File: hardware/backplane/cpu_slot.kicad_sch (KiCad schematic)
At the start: 1 part

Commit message: feat: Re-add peripheral MCLK, add to memory lines (#3)
Need MCLK to maintain peripheral synchronization.  Add missing memory
access size and latch lines.
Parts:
- renumbered J9 to J8
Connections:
- net UART.RX is gone; now on an unnamed net: J8.B13
- net UART.TX is gone; now on net MCLK: J8.B12
- net GND: no longer J8.A16
- net MCLK: no longer J8.B18
- net ~{MRST}: now also J8.A16; no longer J8.B17
- net at J8.B1, J8.B49, J8.B82: no longer J8.B16
- net I2C.SCL: no longer names the net of J8.B14
- net I2C.SDA: no longer names the net of J8.B15
- new net MEM.BYTE: J8.B18
- new net MEM.HALFWORD: J8.B17
- new net MEM.LATCH: J8.B16
- no-connect marks 17 -> 19

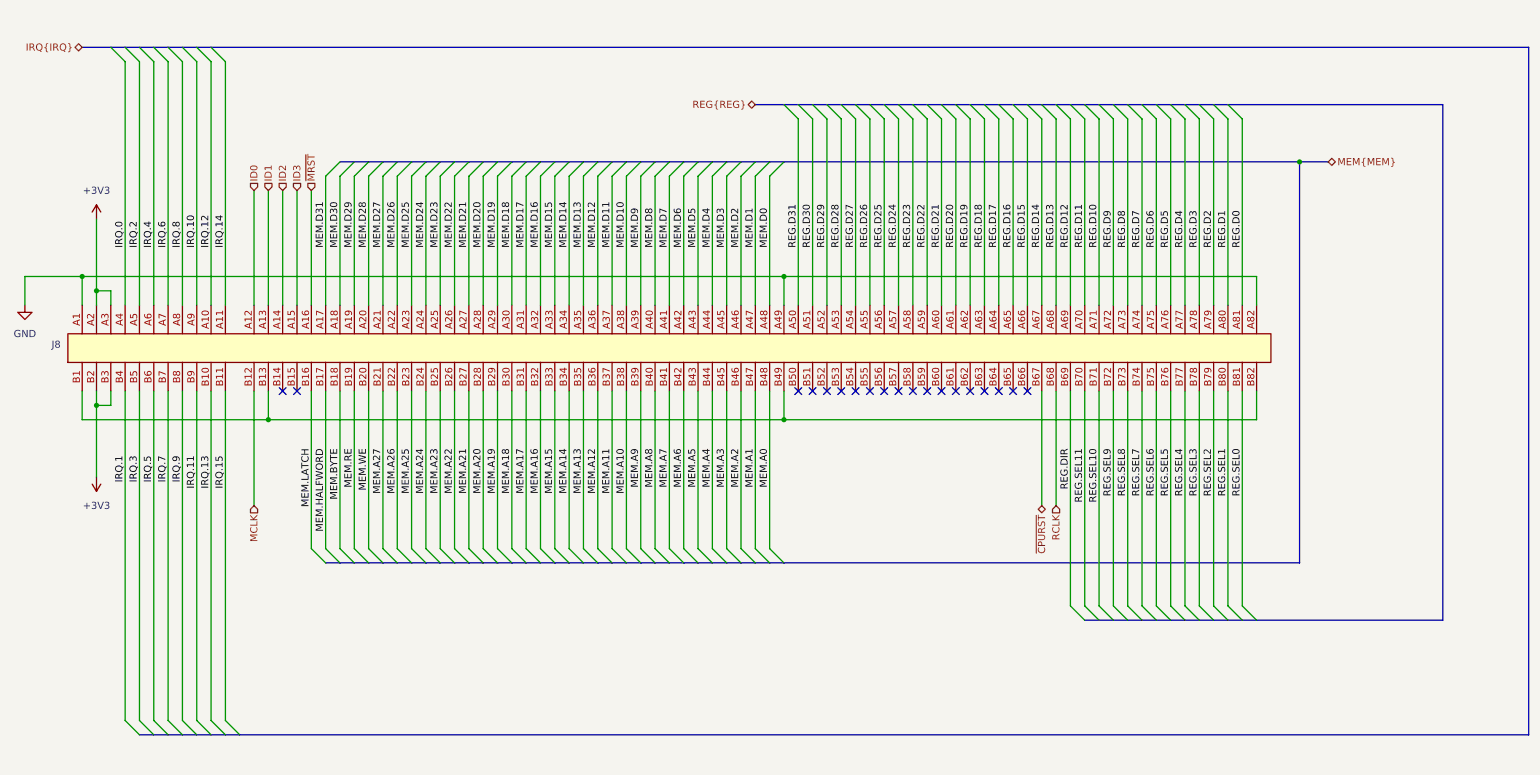
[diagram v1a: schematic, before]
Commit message: feat: Assign footprints, add testpoints
 * Verify all footprints are assigned.
 * Create testpoints for key signals.
 * Reorganize component libraries.
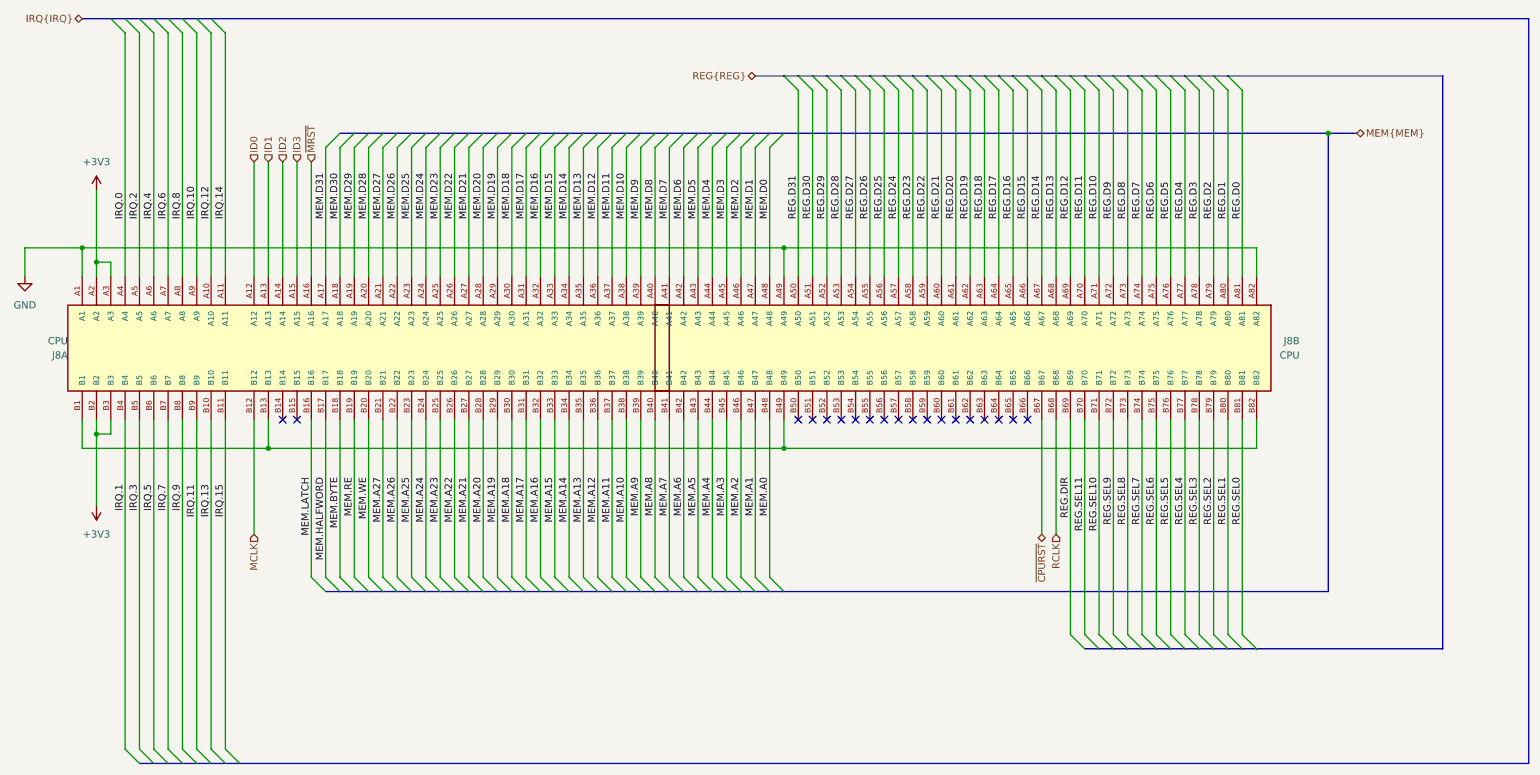
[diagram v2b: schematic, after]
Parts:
- removed J8: ~, symbol Connector_PCIe:PCIe_x16
- added J8: CPU, 10018783_10113TLF:AMPHENOL_10018783-10113TLF, symbol 10018783-10113TLF:10018783-10113TLF
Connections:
- net +3V3: now also J8.A2, J8.A3, J8.B2, J8.B3
- net GND: now also J8.A1, J8.A49, J8.A82
- net ID0: now also J8.A12
- net ID1: now also J8.A13
- net ID2: now also J8.A14
- net ID3: now also J8.A15
- net IRQ.0: now also J8.A4
- net IRQ.1: now also J8.B4
- net IRQ.10: now also J8.A9
- net IRQ.11: now also J8.B9
- net IRQ.12: now also J8.A10
- net IRQ.13: now also J8.B10
- net IRQ.14: now also J8.A11
- net IRQ.15: now also J8.B11
- net IRQ.2: now also J8.A5
- net IRQ.3: now also J8.B5
- net IRQ.4: now also J8.A6
- net IRQ.5: now also J8.B6
- net IRQ.6: now also J8.A7
- net IRQ.7: now also J8.B7
- net IRQ.8: now also J8.A8
- net IRQ.9: now also J8.B8
- net MCLK: now also J8.B12
- net MEM.A0: now also J8.B48
- net MEM.A1: now also J8.B47
- net MEM.A10: now also J8.B38
- net MEM.A11: now also J8.B37
- net MEM.A12: now also J8.B36
- net MEM.A13: now also J8.B35
- net MEM.A14: now also J8.B34
- net MEM.A15: now also J8.B33
- net MEM.A16: now also J8.B32
- net MEM.A17: now also J8.B31
- net MEM.A18: now also J8.B30
- net MEM.A19: now also J8.B29
- net MEM.A2: now also J8.B46
- net MEM.A20: now also J8.B28
- net MEM.A21: now also J8.B27
- net MEM.A22: now also J8.B26
- net MEM.A23: now also J8.B25
- net MEM.A24: now also J8.B24
- net MEM.A25: now also J8.B23
- net MEM.A26: now also J8.B22
- net MEM.A27: now also J8.B21
- net MEM.A3: now also J8.B45
- net MEM.A4: now also J8.B44
- net MEM.A5: now also J8.B43
- net MEM.A6: now also J8.B42
- net MEM.A7: now also J8.B41
- net MEM.A8: now also J8.B40
- net MEM.A9: now also J8.B39
- net MEM.BYTE: now also J8.B18
- net MEM.D0: now also J8.A48
- net MEM.D1: now also J8.A47
- net MEM.D10: now also J8.A38
- net MEM.D11: now also J8.A37
- net MEM.D12: now also J8.A36
- net MEM.D13: now also J8.A35
- net MEM.D14: now also J8.A34
- net MEM.D15: now also J8.A33
- net MEM.D16: now also J8.A32
- net MEM.D17: now also J8.A31
- net MEM.D18: now also J8.A30
- net MEM.D19: now also J8.A29
- net MEM.D2: now also J8.A46
- net MEM.D20: now also J8.A28
- net MEM.D21: now also J8.A27
- net MEM.D22: now also J8.A26
- net MEM.D23: now also J8.A25
- net MEM.D24: now also J8.A24
- net MEM.D25: now also J8.A23
- net MEM.D26: now also J8.A22
- net MEM.D27: now also J8.A21
- net MEM.D28: now also J8.A20
- net MEM.D29: now also J8.A19
- net MEM.D3: now also J8.A45
- net MEM.D30: now also J8.A18
- net MEM.D31: now also J8.A17
- net MEM.D4: now also J8.A44
- net MEM.D5: now also J8.A43
- net MEM.D6: now also J8.A42
- net MEM.D7: now also J8.A41
- net MEM.D8: now also J8.A40
- net MEM.D9: now also J8.A39
- net MEM.HALFWORD: now also J8.B17
- net MEM.LATCH: now also J8.B16
- net MEM.RE: now also J8.B19
- net MEM.WE: now also J8.B20
- net RCLK: now also J8.B68
- net REG.D0: now also J8.A81
- net REG.D1: now also J8.A80
- net REG.D10: now also J8.A71
- net REG.D11: now also J8.A70
- net REG.D12: now also J8.A69
- net REG.D13: now also J8.A68
- net REG.D14: now also J8.A67
- net REG.D15: now also J8.A66
- net REG.D16: now also J8.A65
- net REG.D17: now also J8.A64
- net REG.D18: now also J8.A63
- net REG.D19: now also J8.A62
- net REG.D2: now also J8.A79
- net REG.D20: now also J8.A61
- net REG.D21: now also J8.A60
- net REG.D22: now also J8.A59
- net REG.D23: now also J8.A58
- net REG.D24: now also J8.A57
- net REG.D25: now also J8.A56
- net REG.D26: now also J8.A55
- net REG.D27: now also J8.A54
- net REG.D28: now also J8.A53
- net REG.D29: now also J8.A52
- net REG.D3: now also J8.A78
- net REG.D30: now also J8.A51
- net REG.D31: now also J8.A50
- net REG.D4: now also J8.A77
- net REG.D5: now also J8.A76
- net REG.D6: now also J8.A75
- net REG.D7: now also J8.A74
- net REG.D8: now also J8.A73
- net REG.D9: now also J8.A72
- net REG.DIR: now also J8.B69
- net REG.SEL0: now also J8.B81
- net REG.SEL1: now also J8.B80
- net REG.SEL10: now also J8.B71
- net REG.SEL11: now also J8.B70
- net REG.SEL2: now also J8.B79
- net REG.SEL3: now also J8.B78
- net REG.SEL4: now also J8.B77
- net REG.SEL5: now also J8.B76
- net REG.SEL6: now also J8.B75
- net REG.SEL7: now also J8.B74
- net REG.SEL8: now also J8.B73
- net REG.SEL9: now also J8.B72
- net ~{CPURST}: now also J8.B67
- net ~{MRST}: now also J8.A16
- new net: J8.B1, J8.B13, J8.B49, J8.B82

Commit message: feat: Apply bus arch changes to backplane schematic
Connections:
- net GND: now also J8.B1, J8.B13, J8.B49, J8.B82
- net MEM.~{FAULT}: now reaches J8.B15
- net MEM.BYTE renamed MEM.~{ARDY}
- net MEM.HALFWORD renamed MEM.~{DRDY}
- net MEM.LATCH renamed MEM.~{WR}
- net MEM.RE renamed MEM.HALF0
- net MEM.WE renamed MEM.HALF1
- net REG.DIR renamed REG.~{WR}
- net REG.SEL0 renamed REG.R0
- net REG.SEL1 renamed REG.R1
- net REG.SEL10 renamed REG.R10
- net REG.SEL11 renamed REG.R11
- net REG.SEL2 renamed REG.R2
- net REG.SEL3 renamed REG.R3
- net REG.SEL4 renamed REG.R4
- net REG.SEL5 renamed REG.R5
- net REG.SEL6 renamed REG.R6
- net REG.SEL7 renamed REG.R7
- net REG.SEL8 renamed REG.R8
- net REG.SEL9 renamed REG.R9
- net ~{CPURST} renamed ~{CRST}
- no-connect marks 19 -> 18
